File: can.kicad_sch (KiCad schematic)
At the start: 4 parts, among them J5 Conn_01x04, U8 TCAN3414DRBR

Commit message: 24V Regulator, Pyro Igniter Circuit
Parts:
- renumbered J5 to J13
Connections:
- net CAN_H: now also J13.3 (Pin_3); no longer J13.2 (Pin_2)
- net CAN_L: now also J13.2 (Pin_2); no longer J13.3 (Pin_3)
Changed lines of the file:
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@@
+		)
+	)
+	(label "CAN_H"
+		(at 199.39 104.14 0)
+		(effects
+			(font
+				(size 1.27 1.27)
+			)
+			(justify left bottom)
 		)
 	)
 	(label "CAN_L"
-		(at 199.39 104.14 0)
+		(at 199.39 101.6 0)
 		(effects
 			(font
@@
 			)
 			(justify right bottom)
-		)
-	)
-	(label "CAN_H"
-		(at 199.39 101.6 0)
-		(effects
-			(font
-				(size 1.27 1.27)
-			)
-			(justify left bottom)
 		)
 	)
@@
 		(dnp no)
 		(fields_autoplaced yes)
-		(property "Reference" "J5"
+		(property "Reference" "J13"
 			(at 191.77 92.71 0)
 			(show_name no)
@@
 			(project "mixed_signal_sensor_board"
 				(path "/5c142d60-6b5a-463f-88b9-a177eae7f51b/7c2b22b5-688e-4abb-826f-bfcea6504725"
-					(reference "J5")
+					(reference "J13")
 					(unit 1)
 				)
@@
 		(dnp no)
 		(fields_autoplaced yes)
-		(property "Reference" "#PWR0102"
+		(property "Reference" "#PWR098"
 			(at 142.24 86.36 0)
 			(hide yes)
@@
 			(project "mixed_signal_sensor_board"
 				(path "/5c142d60-6b5a-463f-88b9-a177eae7f51b/7c2b22b5-688e-4abb-826f-bfcea6504725"
-					(reference "#PWR0102")
+					(reference "#PWR098")
 					(unit 1)
 				)
@@
 		(in_pos_files yes)
 		(dnp no)
-		(property "Reference" "#PWR0101"
+		(property "Reference" "#PWR097"
 			(at 143.51 100.33 0)
 			(hide yes)
@@
 			(project "mixed_signal_sensor_board"
 				(path "/5c142d60-6b5a-463f-88b9-a177eae7f51b/7c2b22b5-688e-4abb-826f-bfcea6504725"
-					(reference "#PWR0101")
+					(reference "#PWR097")
 					(unit 1)
 				)
@@
 		(dnp no)
 		(fields_autoplaced yes)
-		(property "Reference" "#PWR099"
+		(property "Reference" "#PWR095"
 			(at 110.49 85.09 0)
 			(hide yes)
@@
 			(project "mixed_signal_sensor_board"
 				(path "/5c142d60-6b5a-463f-88b9-a177eae7f51b/7c2b22b5-688e-4abb-826f-bfcea6504725"
-					(reference "#PWR099")
+					(reference "#PWR095")
 					(unit 1)
 				)
@@
 		(dnp no)
 		(fields_autoplaced yes)
-		(property "Reference" "#PWR056"
+		(property "Reference" "#PWR0100"
 			(at 203.2 106.68 0)
 			(hide yes)
@@
 			(project "mixed_signal_sensor_board"
 				(path "/5c142d60-6b5a-463f-88b9-a177eae7f51b/7c2b22b5-688e-4abb-826f-bfcea6504725"
-					(reference "#PWR056")
+					(reference "#PWR0100")
 					(unit 1)
 				)
@@
 		(dnp no)
 		(fields_autoplaced yes)
-		(property "Reference" "#PWR055"
+		(property "Reference" "#PWR099"
 			(at 193.04 99.06 0)
 			(hide yes)
@@
 			(project "mixed_signal_sensor_board"
 				(path "/5c142d60-6b5a-463f-88b9-a177eae7f51b/7c2b22b5-688e-4abb-826f-bfcea6504725"
-					(reference "#PWR055")
+					(reference "#PWR099")
 					(unit 1)
 				)
@@
 		(in_pos_files yes)
 		(dnp no)
-		(property "Reference" "#PWR0100"
+		(property "Reference" "#PWR096"
 			(at 140.97 118.11 0)
 			(hide yes)
@@
 			(project "mixed_signal_sensor_board"
 				(path "/5c142d60-6b5a-463f-88b9-a177eae7f51b/7c2b22b5-688e-4abb-826f-bfcea6504725"
-					(reference "#PWR0100")
+					(reference "#PWR096")
 					(unit 1)
 				)

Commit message: Pyro fault detection, Decoupling Caps STM32, Initial PCB Layout
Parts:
- J13: footprint Connector_JST:JST_XH_B4B-XH-A_1x04_P2.50mm_Vertical -> Connector_JST:JST_XH_S4B-XH-A_1x04_P2.50mm_Horizontal
- renumbered C47 to C53
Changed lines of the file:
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@@
 			)
 		)
-		(property "Footprint" "Connector_JST:JST_XH_B4B-XH-A_1x04_P2.50mm_Vertical"
+		(property "Footprint" "Connector_JST:JST_XH_S4B-XH-A_1x04_P2.50mm_Horizontal"
 			(at 191.77 101.6 0)
 			(hide yes)
@@
 		(dnp no)
 		(fields_autoplaced yes)
-		(property "Reference" "C47"
+		(property "Reference" "C53"
 			(at 147.32 88.8999 0)
 			(show_name no)
@@
 			(project "mixed_signal_sensor_board"
 				(path "/5c142d60-6b5a-463f-88b9-a177eae7f51b/7c2b22b5-688e-4abb-826f-bfcea6504725"
-					(reference "C47")
+					(reference "C53")
 					(unit 1)
 				)
@@
 		(dnp no)
 		(fields_autoplaced yes)
-		(property "Reference" "#PWR098"
+		(property "Reference" "#PWR0104"
 			(at 142.24 86.36 0)
 			(hide yes)
@@
 			(project "mixed_signal_sensor_board"
 				(path "/5c142d60-6b5a-463f-88b9-a177eae7f51b/7c2b22b5-688e-4abb-826f-bfcea6504725"
-					(reference "#PWR098")
+					(reference "#PWR0104")
 					(unit 1)
 				)
@@
 		(in_pos_files yes)
 		(dnp no)
-		(property "Reference" "#PWR097"
+		(property "Reference" "#PWR0103"
 			(at 143.51 100.33 0)
 			(hide yes)
@@
 			(project "mixed_signal_sensor_board"
 				(path "/5c142d60-6b5a-463f-88b9-a177eae7f51b/7c2b22b5-688e-4abb-826f-bfcea6504725"
-					(reference "#PWR097")
+					(reference "#PWR0103")
 					(unit 1)
 				)
@@
 		(dnp no)
 		(fields_autoplaced yes)
-		(property "Reference" "#PWR095"
+		(property "Reference" "#PWR0101"
 			(at 110.49 85.09 0)
 			(hide yes)
@@
 			(project "mixed_signal_sensor_board"
 				(path "/5c142d60-6b5a-463f-88b9-a177eae7f51b/7c2b22b5-688e-4abb-826f-bfcea6504725"
-					(reference "#PWR095")
+					(reference "#PWR0101")
 					(unit 1)
 				)
@@
 		(dnp no)
 		(fields_autoplaced yes)
-		(property "Reference" "#PWR0100"
+		(property "Reference" "#PWR0106"
 			(at 203.2 106.68 0)
 			(hide yes)
@@
 			(project "mixed_signal_sensor_board"
 				(path "/5c142d60-6b5a-463f-88b9-a177eae7f51b/7c2b22b5-688e-4abb-826f-bfcea6504725"
-					(reference "#PWR0100")
+					(reference "#PWR0106")
 					(unit 1)
 				)
@@
 		(dnp no)
 		(fields_autoplaced yes)
-		(property "Reference" "#PWR099"
+		(property "Reference" "#PWR0105"
 			(at 193.04 99.06 0)
 			(hide yes)
@@
 			(project "mixed_signal_sensor_board"
 				(path "/5c142d60-6b5a-463f-88b9-a177eae7f51b/7c2b22b5-688e-4abb-826f-bfcea6504725"
-					(reference "#PWR099")
+					(reference "#PWR0105")
 					(unit 1)
 				)
@@
 		(in_pos_files yes)
 		(dnp no)
-		(property "Reference" "#PWR096"
+		(property "Reference" "#PWR0102"
 			(at 140.97 118.11 0)
 			(hide yes)
@@
 			(project "mixed_signal_sensor_board"
 				(path "/5c142d60-6b5a-463f-88b9-a177eae7f51b/7c2b22b5-688e-4abb-826f-bfcea6504725"
-					(reference "#PWR096")
-					(unit 1)
-				)
+					(reference "#PWR0102")
+					(unit 1)
+				)

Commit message: Step files, SMD connectors, reduced size
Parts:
- J13: footprint Connector_JST:JST_XH_S4B-XH-A_1x04_P2.50mm_Horizontal -> Connector_JST:JST_PH_S4B-PH-SM4-TB_1x04-1MP_P2.00mm_Horizontal
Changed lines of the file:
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@@
 			)
 		)
-		(property "Footprint" "Connector_JST:JST_XH_S4B-XH-A_1x04_P2.50mm_Horizontal"
+		(property "Footprint" "Connector_JST:JST_PH_S4B-PH-SM4-TB_1x04-1MP_P2.00mm_Horizontal"
 			(at 191.77 101.6 0)
 			(hide yes)

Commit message: Delvin protection, USB ESD protection, 02x06 pin socket
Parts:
- renumbered U8 to U9
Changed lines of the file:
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@@
 		(dnp no)
 		(fields_autoplaced yes)
-		(property "Reference" "U8"
+		(property "Reference" "U9"
 			(at 125.73 78.74 0)
 			(show_name no)
@@
 			(project "mixed_signal_sensor_board"
 				(path "/5c142d60-6b5a-463f-88b9-a177eae7f51b/7c2b22b5-688e-4abb-826f-bfcea6504725"
-					(reference "U8")
+					(reference "U9")
 					(unit 1)
 				)
@@
 		(dnp no)
 		(fields_autoplaced yes)
-		(property "Reference" "#PWR0104"
+		(property "Reference" "#PWR0105"
 			(at 142.24 86.36 0)
 			(hide yes)
@@
 			(project "mixed_signal_sensor_board"
 				(path "/5c142d60-6b5a-463f-88b9-a177eae7f51b/7c2b22b5-688e-4abb-826f-bfcea6504725"
-					(reference "#PWR0104")
+					(reference "#PWR0105")
 					(unit 1)
 				)
@@
 		(in_pos_files yes)
 		(dnp no)
-		(property "Reference" "#PWR0103"
+		(property "Reference" "#PWR0104"
 			(at 143.51 100.33 0)
 			(hide yes)
@@
 			(project "mixed_signal_sensor_board"
 				(path "/5c142d60-6b5a-463f-88b9-a177eae7f51b/7c2b22b5-688e-4abb-826f-bfcea6504725"
-					(reference "#PWR0103")
+					(reference "#PWR0104")
 					(unit 1)
 				)
@@
 		(dnp no)
 		(fields_autoplaced yes)
-		(property "Reference" "#PWR0101"
+		(property "Reference" "#PWR0102"
 			(at 110.49 85.09 0)
 			(hide yes)
@@
 			(project "mixed_signal_sensor_board"
 				(path "/5c142d60-6b5a-463f-88b9-a177eae7f51b/7c2b22b5-688e-4abb-826f-bfcea6504725"
-					(reference "#PWR0101")
+					(reference "#PWR0102")
 					(unit 1)
 				)
@@
 		(dnp no)
 		(fields_autoplaced yes)
-		(property "Reference" "#PWR0106"
+		(property "Reference" "#PWR0107"
 			(at 203.2 106.68 0)
 			(hide yes)
@@
 			(project "mixed_signal_sensor_board"
 				(path "/5c142d60-6b5a-463f-88b9-a177eae7f51b/7c2b22b5-688e-4abb-826f-bfcea6504725"
-					(reference "#PWR0106")
+					(reference "#PWR0107")
 					(unit 1)
 				)
@@
 		(dnp no)
 		(fields_autoplaced yes)
-		(property "Reference" "#PWR0105"
+		(property "Reference" "#PWR0106"
 			(at 193.04 99.06 0)
 			(hide yes)
@@
 			(project "mixed_signal_sensor_board"
 				(path "/5c142d60-6b5a-463f-88b9-a177eae7f51b/7c2b22b5-688e-4abb-826f-bfcea6504725"
-					(reference "#PWR0105")
+					(reference "#PWR0106")
 					(unit 1)
 				)
@@
 		(in_pos_files yes)
 		(dnp no)
-		(property "Reference" "#PWR0102"
+		(property "Reference" "#PWR0103"
 			(at 140.97 118.11 0)
 			(hide yes)
@@
 			(project "mixed_signal_sensor_board"
 				(path "/5c142d60-6b5a-463f-88b9-a177eae7f51b/7c2b22b5-688e-4abb-826f-bfcea6504725"
-					(reference "#PWR0102")
+					(reference "#PWR0103")
 					(unit 1)
 				)

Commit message: replaced signal blocks, shortening board, adding precise positioning
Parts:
- renumbered J13 to J14, R50 to R51
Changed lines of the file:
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@@
 		(dnp no)
 		(fields_autoplaced yes)
-		(property "Reference" "J13"
+		(property "Reference" "J14"
 			(at 191.77 92.71 0)
 			(show_name no)
@@
 			(project "mixed_signal_sensor_board"
 				(path "/5c142d60-6b5a-463f-88b9-a177eae7f51b/7c2b22b5-688e-4abb-826f-bfcea6504725"
-					(reference "J13")
+					(reference "J14")
 					(unit 1)
 				)
@@
 		(dnp no)
 		(fields_autoplaced yes)
-		(property "Reference" "#PWR0105"
+		(property "Reference" "#PWR0110"
 			(at 142.24 86.36 0)
 			(hide yes)
@@
 			(project "mixed_signal_sensor_board"
 				(path "/5c142d60-6b5a-463f-88b9-a177eae7f51b/7c2b22b5-688e-4abb-826f-bfcea6504725"
-					(reference "#PWR0105")
+					(reference "#PWR0110")
 					(unit 1)
 				)
@@
 		(in_pos_files yes)
 		(dnp no)
-		(property "Reference" "#PWR0104"
+		(property "Reference" "#PWR0109"
 			(at 143.51 100.33 0)
 			(hide yes)
@@
 			(project "mixed_signal_sensor_board"
 				(path "/5c142d60-6b5a-463f-88b9-a177eae7f51b/7c2b22b5-688e-4abb-826f-bfcea6504725"
-					(reference "#PWR0104")
+					(reference "#PWR0109")
 					(unit 1)
 				)
@@
 		(dnp no)
 		(fields_autoplaced yes)
-		(property "Reference" "#PWR0102"
+		(property "Reference" "#PWR0107"
 			(at 110.49 85.09 0)
 			(hide yes)
@@
 			(project "mixed_signal_sensor_board"
 				(path "/5c142d60-6b5a-463f-88b9-a177eae7f51b/7c2b22b5-688e-4abb-826f-bfcea6504725"
-					(reference "#PWR0102")
+					(reference "#PWR0107")
 					(unit 1)
 				)
@@
 		(dnp no)
 		(fields_autoplaced yes)
-		(property "Reference" "#PWR0107"
+		(property "Reference" "#PWR0112"
 			(at 203.2 106.68 0)
 			(hide yes)
@@
 			(project "mixed_signal_sensor_board"
 				(path "/5c142d60-6b5a-463f-88b9-a177eae7f51b/7c2b22b5-688e-4abb-826f-bfcea6504725"
-					(reference "#PWR0107")
+					(reference "#PWR0112")
 					(unit 1)
 				)
@@
 		(in_pos_files yes)
 		(dnp no)
-		(property "Reference" "R50"
+		(property "Reference" "R51"
 			(at 168.91 98.298 90)
 			(show_name no)
@@
 			(project "mixed_signal_sensor_board"
 				(path "/5c142d60-6b5a-463f-88b9-a177eae7f51b/7c2b22b5-688e-4abb-826f-bfcea6504725"
-					(reference "R50")
+					(reference "R51")
 					(unit 1)
 				)
@@
 		(dnp no)
 		(fields_autoplaced yes)
-		(property "Reference" "#PWR0106"
+		(property "Reference" "#PWR0111"
 			(at 193.04 99.06 0)
 			(hide yes)
@@
 			(project "mixed_signal_sensor_board"
 				(path "/5c142d60-6b5a-463f-88b9-a177eae7f51b/7c2b22b5-688e-4abb-826f-bfcea6504725"
-					(reference "#PWR0106")
+					(reference "#PWR0111")
 					(unit 1)
 				)
@@
 		(in_pos_files yes)
 		(dnp no)
-		(property "Reference" "#PWR0103"
+		(property "Reference" "#PWR0108"
 			(at 140.97 118.11 0)
 			(hide yes)
@@
 			(project "mixed_signal_sensor_board"
 				(path "/5c142d60-6b5a-463f-88b9-a177eae7f51b/7c2b22b5-688e-4abb-826f-bfcea6504725"
-					(reference "#PWR0103")
-					(unit 1)
-				)
+					(reference "#PWR0108")
+					(unit 1)
+				)

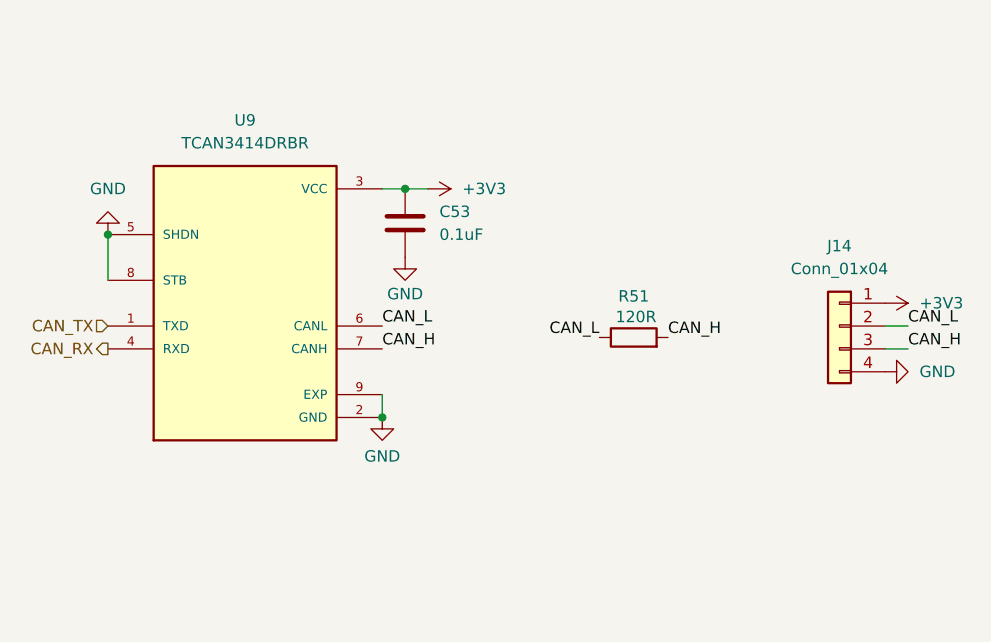
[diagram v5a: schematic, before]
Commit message: PYRO done, schematic structure/convention update, pyro and reverse polarity components selected
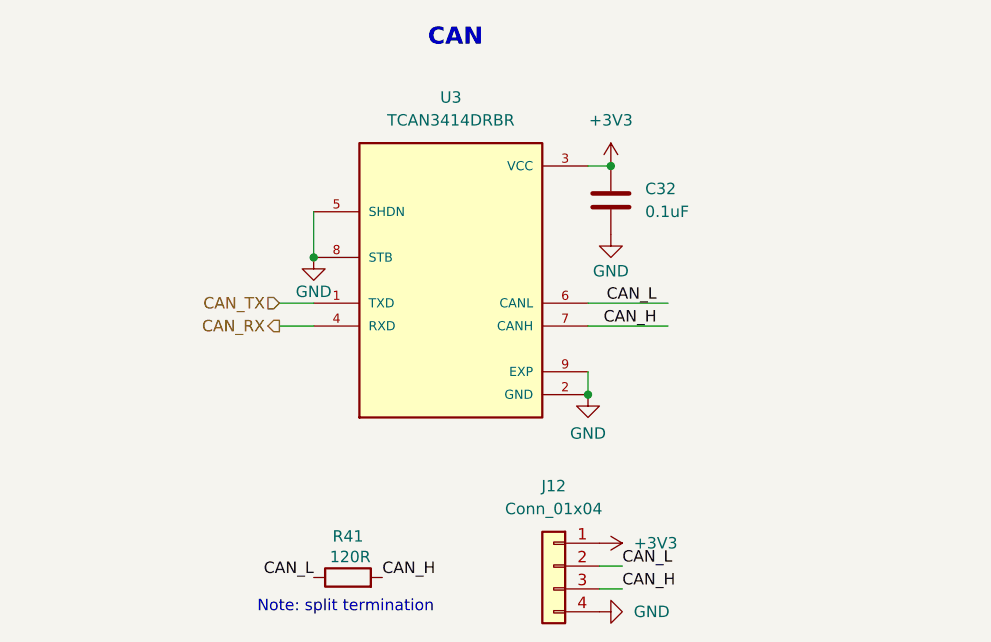
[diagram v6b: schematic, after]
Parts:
- renumbered C53 to C32, J14 to J12, R51 to R41, U9 to U3
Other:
- note added: "CAN"
- note added: "Note: split termination"
- moved on the sheet: C32, J12, R41, U3
